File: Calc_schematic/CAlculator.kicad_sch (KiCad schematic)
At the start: 29 parts, among them SW0 SW_Push, SW1 SW_Push, SW10 SW_Push, SW11 SW_Push, SW12 SW_Push, SW13 SW_Push, SW14 SW_Push, SW15 SW_Push, SW16 SW_Push, SW17 SW_Push, SW18 SW_Push, SW19 SW_Push, SW2 SW_Push, SW20 SW_Push, SW21 SW_Push, SW22 SW_Push, SW23 SW_Push, SW24 SW_Push, SW3 SW_Push, SW4 SW_Push, SW5 SW_Push, SW6 SW_Push, SW7 SW_Push, SW8 SW_Push, SW9 SW_Push, U1 Pico, U2 LCD-016N002L

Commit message: updated
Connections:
- net GND: now also U1.13 (GND), U1.3 (GND), U1.8 (GND)
- net Row3: now reaches SW12.2, SW17.2, SW2.2, SW22.2, SW7.2
- net Row3: now also U1.4 (GPIO2)
- net Col3: now reaches SW15.1, SW16.1, SW17.1, SW18.1, SW19.1
- net Col3: now also U1.10 (GPIO7)
- net Row2: now reaches SW1.2, SW11.2, SW16.2, SW21.2, SW6.2
- net Row2: now also U1.2 (GPIO1)
- net Row4: now reaches SW13.2, SW18.2, SW23.2, SW3.2, SW8.2
- net Row4: now also U1.5 (GPIO3)
- net Col1: now reaches SW0.1, SW1.1, SW2.1, SW3.1, SW4.1
- net Col1: now also U1.7 (GPIO5)
- net Col5: now reaches SW20.1, SW21.1, SW22.1, SW23.1, SW24.1
- net Col5: now also U1.12 (GPIO9)
- net Col4: now reaches SW0.2, SW10.2, SW15.2, SW20.2, SW5.2
- net Col4: now also U1.1 (GPIO0), U1.11 (GPIO8)
- net Col2: now reaches SW5.1, SW6.1, SW7.1, SW8.1, SW9.1
- net Col2: now also U1.9 (GPIO6)
- net Row5: now reaches SW14.2, SW19.2, SW24.2, SW4.2, SW9.2
- net Row5: now also U1.6 (GPIO4)

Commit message: last mod
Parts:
- removed U2: LCD-016N002L, Display:LCD-016N002L, symbol Display_Character:LCD-016N002L
- added U2: PCF8574TS, Package_SO:SSOP-20_4.4x6.5mm_P0.65mm, symbol Interface_Expansion:PCF8574TS
- SW0, SW1, SW10, SW11, SW12, SW13, SW14, SW15, SW16, SW17, SW18, SW19, SW2, SW20, SW21, SW22, SW23, SW24, SW3, SW4, SW5, SW6, SW7, SW8, SW9: footprint (none) -> Button_Switch_THT:SW_PUSH_6mm_H5mm
- U1: footprint RPi_Pico:RPi_Pico_SMD_TH -> MCU_RaspberryPi_and_Boards:RPi_Pico_SMD_TH
- gave numbers to parts that had none: 2
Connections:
- net GND: now also U2.15 (VSS)
- net SDA: now reaches U1.19 (GPIO14)
- net SDA: now also U2.4 (SDA)
- net SCL: now reaches U1.20 (GPIO15)
- net SCL: now also U2.2 (SCL)
- new net 5V: U2.5 (VDD)
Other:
- note added: "LCD Screen i2c controller"
- note added: "We going to use a i2c controller for the LCD screen instead for less pins usage"
- note removed: "LCD Screen"

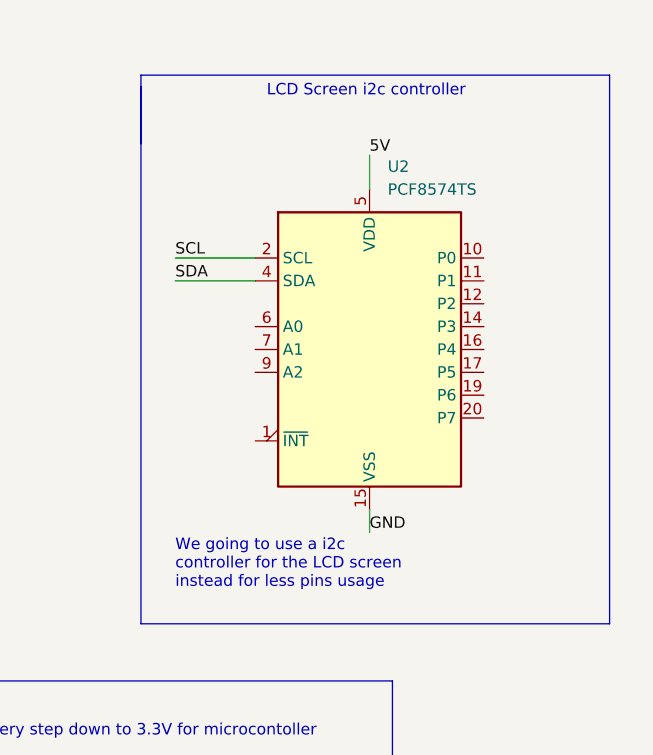
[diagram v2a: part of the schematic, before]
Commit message: updated i2c controller
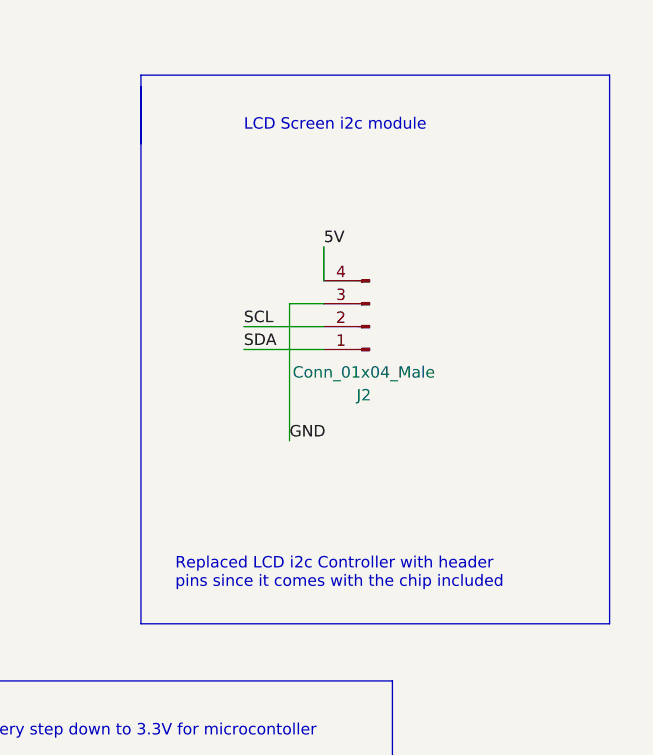
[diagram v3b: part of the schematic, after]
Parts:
- removed U2: PCF8574TS, Package_SO:SSOP-20_4.4x6.5mm_P0.65mm, symbol Interface_Expansion:PCF8574TS
- added J2: Conn_01x04_Male, Connector_PinHeader_2.54mm:PinHeader_1x04_P2.54mm_Vertical, symbol Connector:Conn_01x04_Male
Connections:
- net 5V: now also J2.4 (Pin_4)
- net GND: now also J2.3 (Pin_3)
- net SCL: now also J2.2 (Pin_2)
- net SDA: now also J2.1 (Pin_1)
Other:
- note added: "LCD Screen i2c module"
- note added: "Replaced LCD i2c Controller with header pins since it comes with the chip included"
- note removed: "LCD Screen i2c controller"
- note removed: "We going to use a i2c controller for the LCD screen instead for less pins usage"
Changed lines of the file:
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@@
+    (stroke (width 0) (type default) (color 0 0 0 0))
+  )
+  (wire (pts (xy 222.25 57.15) (xy 222.25 72.39))
     (stroke (width 0) (type default) (color 0 0 0 0))
   )
@@
     (stroke (width 0) (type default) (color 0 0 0 0))
   )
-  (wire (pts (xy 231.14 80.01) (xy 231.14 82.55))
-    (stroke (width 0) (type default) (color 0 0 0 0))
-  )
   (polyline (pts (xy 257.81 92.71) (xy 257.81 31.75))
     (stroke (width 0) (type default) (color 0 0 0 0))
@@
     (stroke (width 0) (type default) (color 0 0 0 0))
   )
-  (wire (pts (xy 209.55 54.61) (xy 218.44 54.61))
+  (wire (pts (xy 217.17 62.23) (xy 226.06 62.23))
     (stroke (width 0) (type default) (color 0 0 0 0))
   )
@@
     (stroke (width 0) (type default) (color 0 0 0 0))
   )
+  (wire (pts (xy 226.06 57.15) (xy 222.25 57.15))
+    (stroke (width 0) (type default) (color 0 0 0 0))
+  )
   (wire (pts (xy 125.73 87.63) (xy 148.59 87.63))
     (stroke (width 0) (type default) (color 0 0 0 0))
@@
     (stroke (width 0) (type default) (color 0 0 0 0))
   )
-  (wire (pts (xy 231.14 40.64) (xy 231.14 44.45))
+  (wire (pts (xy 226.06 50.8) (xy 226.06 54.61))
     (stroke (width 0) (type default) (color 0 0 0 0))
   )
@@
     (stroke (width 0) (type default) (color 0 0 0 0))
   )
-  (wire (pts (xy 209.55 52.07) (xy 218.44 52.07))
+  (wire (pts (xy 217.17 59.69) (xy 226.06 59.69))
     (stroke (width 0) (type default) (color 0 0 0 0))
   )
@@
     (stroke (width 0) (type default) (color 0 0 0 0))
   )
-  (text "LCD Screen i2c controller" (at 219.71 34.29 0)
+  (text "LCD Screen i2c module" (at 217.17 38.1 0)
     (effects (font (size 1.27 1.27)) (justify left bottom))
   )
@@
     (effects (font (size 1.27 1.27)) (justify left bottom))
   )
-  (text "We going to use a i2c\ncontroller for the LCD screen \ninstead for less pins usage"
+  (text "Replaced LCD i2c Controller with header\npins since it comes with the chip included"
     (at 209.55 88.9 0)
     (effects (font (size 1.27 1.27)) (justify left bottom))
@@
     (effects (font (size 1.27 1.27)) (justify left bottom))
   )
+  (label "GND" (at 222.25 72.39 0)
+    (effects (font (size 1.27 1.27)) (justify left bottom))
+  )
   (label "Row1" (at 86.36 29.21 0)
     (effects (font (size 1.27 1.27)) (justify left bottom))
@@
     (effects (font (size 1.27 1.27)) (justify left bottom))
   )
-  (label "GND" (at 231.14 82.55 0)
-    (effects (font (size 1.27 1.27)) (justify left bottom))
-  )
   (label "GND" (at 74.93 135.89 0)
     (effects (font (size 1.27 1.27)) (justify left bottom))
@@
     (effects (font (size 1.27 1.27)) (justify left bottom))
   )
-  (label "SDA" (at 209.55 54.61 0)
+  (label "SDA" (at 217.17 62.23 0)
     (effects (font (size 1.27 1.27)) (justify left bottom))
   )
@@
     (effects (font (size 1.27 1.27)) (justify left bottom))
   )
-  (label "SCL" (at 209.55 52.07 0)
+  (label "SCL" (at 217.17 59.69 0)
     (effects (font (size 1.27 1.27)) (justify left bottom))
   )
@@
     (effects (font (size 1.27 1.27)) (justify left bottom))
   )
-  (label "5V" (at 231.14 40.64 0)
+  (label "5V" (at 226.06 50.8 0)
     (effects (font (size 1.27 1.27)) (justify left bottom))
   )
@@
     (pin "2")
   )
+  (symbol (lib_id "Connector:Conn_01x04_Male") (at 231.14 59.69 180) (unit 1)
+    (in_bom yes) (on_board yes) (fields_autoplaced)
+    (property "Reference" "J2" (id 0) (at 230.505 67.31 0))
+    (property "Value" "Conn_01x04_Male" (id 1) (at 230.505 64.77 0))
+    (property "Footprint" "Connector_PinHeader_2.54mm:PinHeader_1x04_P2.54mm_Vertical" (id 2) (at 231.14 59.69 0)
+      (effects (font (size 1.27 1.27)) hide)
+    )
+    (property "Datasheet" "~" (id 3) (at 231.14 59.69 0)
+      (effects (font (size 1.27 1.27)) hide)
+    )
+    (pin "1")
+    (pin "2")
+    (pin "3")
+    (pin "4")
+  )
   (symbol (lib_id "Switch:SW_Push") (at 55.88 81.28 0) (unit 1)
     (in_bom yes) (on_board yes) (fields_autoplaced)
@@
     (pin "2")
   )
-  (symbol (lib_id "Interface_Expansion:PCF8574TS") (at 231.14 62.23 0) (unit 1)
-    (in_bom yes) (on_board yes) (fields_autoplaced)
-    (property "Reference" "U2" (id 0) (at 233.1594 41.91 0)
-      (effects (font (size 1.27 1.27)) (justify left))
-    )
-    (property "Value" "PCF8574TS" (id 1) (at 233.1594 44.45 0)
-      (effects (font (size 1.27 1.27)) (justify left))
-    )
-    (property "Footprint" "Package_SO:SSOP-20_4.4x6.5mm_P0.65mm" (id 2) (at 231.14 62.23 0)
-      (effects (font (size 1.27 1.27)) hide)
-    )
-    (property "Datasheet" "http://www.nxp.com/documents/data_sheet/PCF8574_PCF8574A.pdf" (id 3) (at 231.14 62.23 0)
-      (effects (font (size 1.27 1.27)) hide)
-    )
-    (pin "1")
-    (pin "10")
-    (pin "11")
-    (pin "12")
-    (pin "13")
-    (pin "14")
-    (pin "15")
-    (pin "16")
-    (pin "17")
-    (pin "18")
-    (pin "19")
-    (pin "2")
-    (pin "20")
-    (pin "3")
-    (pin "4")
-    (pin "5")
-    (pin "6")
-    (pin "7")
-    (pin "8")
-    (pin "9")
-  )
   (sheet_instances
     (path "/" (page "1"))
@@
       (reference "J1") (unit 1) (value "Conn_01x02_Female") (footprint "Connector_JST:JST_PH_B2B-PH-K_1x02_P2.00mm_Vertical")
     )
+    (path "/ac4c7e2c-99b9-4041-8d62-1831c048dcf9"
+      (reference "J2") (unit 1) (value "Conn_01x04_Male") (footprint "Connector_PinHeader_2.54mm:PinHeader_1x04_P2.54mm_Vertical")
+    )
     (path "/ee20195a-d192-4730-87d7-a0b36c6295af"
       (reference "SW0") (unit 1) (value "SW_Push") (footprint "Button_Switch_THT:SW_PUSH_6mm_H5mm")
@@
       (reference "U1") (unit 1) (value "Pico") (footprint "MCU_RaspberryPi_and_Boards:RPi_Pico_SMD_TH")
     )
-    (path "/f9bc0e2e-b866-4474-96af-9520a16e439e"
-      (reference "U2") (unit 1) (value "PCF8574TS") (footprint "Package_SO:SSOP-20_4.4x6.5mm_P0.65mm")
-    )
     (path "/4b36419b-4a98-41ad-a571-a91a011b3792"

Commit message: most pins connected except Vbus and ground
Going to use ground plane so no need to connect ground pins yet
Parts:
- removed U3: AP2112K-3.3, Package_TO_SOT_SMD:SOT-23-5, symbol Regulator_Linear:AP2112K-3.3
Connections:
- net 5V: now also U1.40 (VBUS)
- net Col3: now also SW10.1, SW11.1, SW12.1, SW13.1, SW14.1; no longer SW15.1, SW16.1, SW17.1, SW18.1, SW19.1
- net Col4: now also SW15.1, SW16.1, SW17.1, SW18.1, SW19.1; no longer SW0.2, SW10.2, SW15.2, SW20.2, SW5.2, U1.1 (GPIO0)
- net GND: now also U1.18 (GND), U1.23 (GND), U1.38 (GND)
- new net Row1: SW0.2, SW10.2, SW15.2, SW20.2, SW5.2, U1.1 (GPIO0)
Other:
- note added: "5V input volatge from lipo battery"
- note removed: "5V from lipo battery step down to 3.3V for microcontoller"
- note removed: "Power Supply"
- moved on the sheet: J1

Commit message: final CAD
board sent to FaB
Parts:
- added R1, R10, R2, R3, R4, R5, R6, R7, R8, R9: R, SamacSys_Parts:RESC3216X60N, symbol Device:R
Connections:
- net Col1: now also R2.2
- net Col2: now also R3.2
- net Col3: now also R10.1
- net Col4: now also R6.2
- net Col5: now also R7.2
- net GND: now also J1.2 (Pin_2), R1.2, R10.2, R2.1, R3.1, R4.1, R5.1, R6.1, R7.1, R8.1, R9.2
- net Row1: now also R4.2
- net Row2: now also R9.1
- net Row3: now also R1.1
- net Row4: now also R8.2
- net Row5: now also R5.2
- net VBAT: now reaches U1.39 (VSYS)
- net VBAT: now also J1.1 (Pin_1)
- no-connect marks 0 -> 18
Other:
- moved on the sheet: J1
